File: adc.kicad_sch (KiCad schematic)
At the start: 9 parts, among them U801 AD7357xRU

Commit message: Combined update (kicad 6.0.4..) - Update schematic to kicad 6.0.4 - Assign footprints for SMA connectors - Replace MCP1825T with MCP1824T (chip shortages..)
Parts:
- renumbered C801 to C701, C802 to C702, C803 to C703, C804 to C704, C805 to C705, C806 to C706, C807 to C707, C808 to C708, U801 to U701
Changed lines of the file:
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@@
     (effects (font (size 1.27 1.27)) (justify right))
   )
-  (symbol (lib_id "symbols:+3.3VD") (at 167.64 38.1 0)
-    (in_bom yes) (on_board yes) (fields_autoplaced)
-    (property "Reference" "#PWR0810" (id 0) (at 167.64 41.91 0)
+  (symbol (lib_id "symbols:+3.3VD") (at 167.64 38.1 0) (unit 1)
+    (in_bom yes) (on_board yes) (fields_autoplaced)
+    (property "Reference" "#PWR0710" (id 0) (at 167.64 41.91 0)
       (effects (font (size 1.27 1.27)) hide)
     )
@@
     (pin "1")
   )
-  (symbol (lib_id "Device:C_Polarized") (at 120.65 125.73 0)
-    (in_bom yes) (on_board yes) (fields_autoplaced)
-    (property "Reference" "C802" (id 0) (at 123.571 124.0063 0)
+  (symbol (lib_id "Device:C_Polarized") (at 120.65 125.73 0) (unit 1)
+    (in_bom yes) (on_board yes) (fields_autoplaced)
+    (property "Reference" "C702" (id 0) (at 123.571 124.0063 0)
       (effects (font (size 1.27 1.27)) (justify left))
     )
@@
     (pin "2")
   )
-  (symbol (lib_id "Device:C") (at 133.35 95.25 0)
-    (in_bom yes) (on_board yes) (fields_autoplaced)
-    (property "Reference" "C803" (id 0) (at 136.271 94.4153 0)
+  (symbol (lib_id "Device:C") (at 133.35 95.25 0) (unit 1)
+    (in_bom yes) (on_board yes) (fields_autoplaced)
+    (property "Reference" "C703" (id 0) (at 136.271 94.4153 0)
       (effects (font (size 1.27 1.27)) (justify left))
     )
@@
     (pin "2")
   )
-  (symbol (lib_id "symbols:AD7357xRU") (at 158.75 101.6 0)
-    (in_bom yes) (on_board yes) (fields_autoplaced)
-    (property "Reference" "U801" (id 0) (at 164.5794 72.6272 0)
+  (symbol (lib_id "symbols:AD7357xRU") (at 158.75 101.6 0) (unit 1)
+    (in_bom yes) (on_board yes) (fields_autoplaced)
+    (property "Reference" "U701" (id 0) (at 164.5794 72.6272 0)
       (effects (font (size 1.27 1.27)) (justify left))
     )
@@
     (pin "9")
   )
-  (symbol (lib_id "power:GND") (at 120.65 130.81 0)
-    (in_bom yes) (on_board yes) (fields_autoplaced)
-    (property "Reference" "#PWR0802" (id 0) (at 120.65 137.16 0)
+  (symbol (lib_id "power:GND") (at 120.65 130.81 0) (unit 1)
+    (in_bom yes) (on_board yes) (fields_autoplaced)
+    (property "Reference" "#PWR0702" (id 0) (at 120.65 137.16 0)
       (effects (font (size 1.27 1.27)) hide)
     )
@@
     (pin "1")
   )
-  (symbol (lib_id "Device:C") (at 133.35 125.73 0)
-    (in_bom yes) (on_board yes) (fields_autoplaced)
-    (property "Reference" "C804" (id 0) (at 136.271 124.8953 0)
+  (symbol (lib_id "Device:C") (at 133.35 125.73 0) (unit 1)
+    (in_bom yes) (on_board yes) (fields_autoplaced)
+    (property "Reference" "C704" (id 0) (at 136.271 124.8953 0)
       (effects (font (size 1.27 1.27)) (justify left))
     )
@@
     (pin "2")
   )
-  (symbol (lib_id "power:GND") (at 120.65 100.33 0)
-    (in_bom yes) (on_board yes) (fields_autoplaced)
-    (property "Reference" "#PWR0801" (id 0) (at 120.65 106.68 0)
+  (symbol (lib_id "power:GND") (at 120.65 100.33 0) (unit 1)
+    (in_bom yes) (on_board yes) (fields_autoplaced)
+    (property "Reference" "#PWR0701" (id 0) (at 120.65 106.68 0)
       (effects (font (size 1.27 1.27)) hide)
     )
@@
     (pin "1")
   )
-  (symbol (lib_id "Device:C") (at 149.86 44.45 0)
-    (in_bom yes) (on_board yes) (fields_autoplaced)
-    (property "Reference" "C806" (id 0) (at 152.781 43.6153 0)
+  (symbol (lib_id "Device:C") (at 149.86 44.45 0) (unit 1)
+    (in_bom yes) (on_board yes) (fields_autoplaced)
+    (property "Reference" "C706" (id 0) (at 152.781 43.6153 0)
       (effects (font (size 1.27 1.27)) (justify left))
     )
@@
     (pin "2")
   )
-  (symbol (lib_id "power:GND") (at 149.86 50.8 0)
-    (in_bom yes) (on_board yes) (fields_autoplaced)
-    (property "Reference" "#PWR0806" (id 0) (at 149.86 57.15 0)
+  (symbol (lib_id "power:GND") (at 149.86 50.8 0) (unit 1)
+    (in_bom yes) (on_board yes) (fields_autoplaced)
+    (property "Reference" "#PWR0706" (id 0) (at 149.86 57.15 0)
       (effects (font (size 1.27 1.27)) hide)
     )
@@
     (pin "1")
   )
-  (symbol (lib_id "symbols:+2.5VA") (at 154.94 72.39 0)
-    (in_bom yes) (on_board yes) (fields_autoplaced)
-    (property "Reference" "#PWR0808" (id 0) (at 154.94 76.2 0)
+  (symbol (lib_id "symbols:+2.5VA") (at 154.94 72.39 0) (unit 1)
+    (in_bom yes) (on_board yes) (fields_autoplaced)
+    (property "Reference" "#PWR0708" (id 0) (at 154.94 76.2 0)
       (effects (font (size 1.27 1.27)) hide)
     )
@@
     (pin "1")
   )
-  (symbol (lib_id "symbols:+3.3VD") (at 162.56 72.39 0)
-    (in_bom yes) (on_board yes) (fields_autoplaced)
-    (property "Reference" "#PWR0809" (id 0) (at 162.56 76.2 0)
+  (symbol (lib_id "symbols:+3.3VD") (at 162.56 72.39 0) (unit 1)
+    (in_bom yes) (on_board yes) (fields_autoplaced)
+    (property "Reference" "#PWR0709" (id 0) (at 162.56 76.2 0)
       (effects (font (size 1.27 1.27)) hide)
     )
@@
     (pin "1")
   )
-  (symbol (lib_id "power:GND") (at 133.35 130.81 0)
-    (in_bom yes) (on_board yes) (fields_autoplaced)
-    (property "Reference" "#PWR0804" (id 0) (at 133.35 137.16 0)
+  (symbol (lib_id "power:GND") (at 133.35 130.81 0) (unit 1)
+    (in_bom yes) (on_board yes) (fields_autoplaced)
+    (property "Reference" "#PWR0704" (id 0) (at 133.35 137.16 0)
       (effects (font (size 1.27 1.27)) hide)
     )
@@
     (pin "1")
   )
-  (symbol (lib_id "power:GND") (at 167.64 50.8 0)
-    (in_bom yes) (on_board yes) (fields_autoplaced)
-    (property "Reference" "#PWR0811" (id 0) (at 167.64 57.15 0)
+  (symbol (lib_id "power:GND") (at 167.64 50.8 0) (unit 1)
+    (in_bom yes) (on_board yes) (fields_autoplaced)
+    (property "Reference" "#PWR0711" (id 0) (at 167.64 57.15 0)
       (effects (font (size 1.27 1.27)) hide)
     )
@@
     (pin "1")
   )
-  (symbol (lib_id "Device:C_Polarized") (at 120.65 95.25 0)
-    (in_bom yes) (on_board yes) (fields_autoplaced)
-    (property "Reference" "C801" (id 0) (at 123.571 93.5263 0)
+  (symbol (lib_id "Device:C_Polarized") (at 120.65 95.25 0) (unit 1)
+    (in_bom yes) (on_board yes) (fields_autoplaced)
+    (property "Reference" "C701" (id 0) (at 123.571 93.5263 0)
       (effects (font (size 1.27 1.27)) (justify left))
     )
@@
     (pin "2")
   )
-  (symbol (lib_id "symbols:+2.5VA") (at 149.86 38.1 0)
-    (in_bom yes) (on_board yes) (fields_autoplaced)
-    (property "Reference" "#PWR0805" (id 0) (at 149.86 41.91 0)
+  (symbol (lib_id "symbols:+2.5VA") (at 149.86 38.1 0) (unit 1)
+    (in_bom yes) (on_board yes) (fields_autoplaced)
+    (property "Reference" "#PWR0705" (id 0) (at 149.86 41.91 0)
       (effects (font (size 1.27 1.27)) hide)
     )
@@
     (pin "1")
   )
-  (symbol (lib_id "Device:C") (at 180.34 44.45 0)
-    (in_bom yes) (on_board yes) (fields_autoplaced)
-    (property "Reference" "C808" (id 0) (at 183.261 43.6153 0)
+  (symbol (lib_id "Device:C") (at 180.34 44.45 0) (unit 1)
+    (in_bom yes) (on_board yes) (fields_autoplaced)
+    (property "Reference" "C708" (id 0) (at 183.261 43.6153 0)
       (effects (font (size 1.27 1.27)) (justify left))
     )
@@
     (pin "2")
   )
-  (symbol (lib_id "Device:C") (at 167.64 44.45 0)
-    (in_bom yes) (on_board yes) (fields_autoplaced)
-    (property "Reference" "C807" (id 0) (at 170.561 43.6153 0)
+  (symbol (lib_id "Device:C") (at 167.64 44.45 0) (unit 1)
+    (in_bom yes) (on_board yes) (fields_autoplaced)
+    (property "Reference" "C707" (id 0) (at 170.561 43.6153 0)
       (effects (font (size 1.27 1.27)) (justify left))
     )
@@
     (pin "2")
   )
-  (symbol (lib_id "Device:C") (at 137.16 44.45 0)
-    (in_bom yes) (on_board yes) (fields_autoplaced)
-    (property "Reference" "C805" (id 0) (at 140.081 43.6153 0)
+  (symbol (lib_id "Device:C") (at 137.16 44.45 0) (unit 1)
+    (in_bom yes) (on_board yes) (fields_autoplaced)
+    (property "Reference" "C705" (id 0) (at 140.081 43.6153 0)
       (effects (font (size 1.27 1.27)) (justify left))
     )
@@
     (pin "2")
   )
-  (symbol (lib_id "power:GND") (at 153.67 132.08 0)
-    (in_bom yes) (on_board yes) (fields_autoplaced)
-    (property "Reference" "#PWR0807" (id 0) (at 153.67 138.43 0)
+  (symbol (lib_id "power:GND") (at 153.67 132.08 0) (unit 1)
+    (in_bom yes) (on_board yes) (fields_autoplaced)
+    (property "Reference" "#PWR0707" (id 0) (at 153.67 138.43 0)
       (effects (font (size 1.27 1.27)) hide)
     )
@@
     (pin "1")
   )
-  (symbol (lib_id "power:GND") (at 133.35 100.33 0)
-    (in_bom yes) (on_board yes) (fields_autoplaced)
-    (property "Reference" "#PWR0803" (id 0) (at 133.35 106.68 0)
-      (effects (font (size 1.27 1.27)) hide)
-    )
+  (symbol (lib_id "power:GND") (at 133.35 100.33 0) (unit 1)
+    (in_bom yes) (on_board yes) (fields_autoplaced)
+    (property "Reference" "#PWR0703" (id 0) (at 133.35 106.68 0)
+      (effects (font (size 1.27 1.27)) hide)
+    )

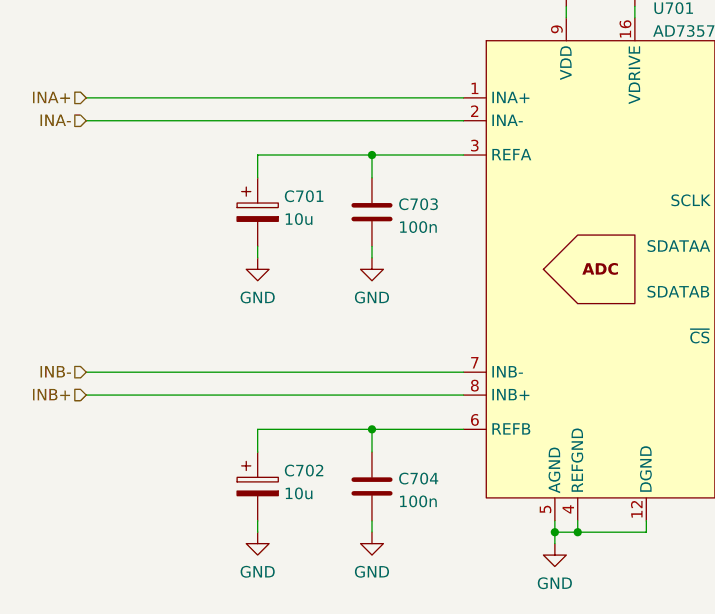
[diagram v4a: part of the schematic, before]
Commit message: Replace 10uf al-elco by tantalum -Space savings (0805 vs 4mm cylinder)
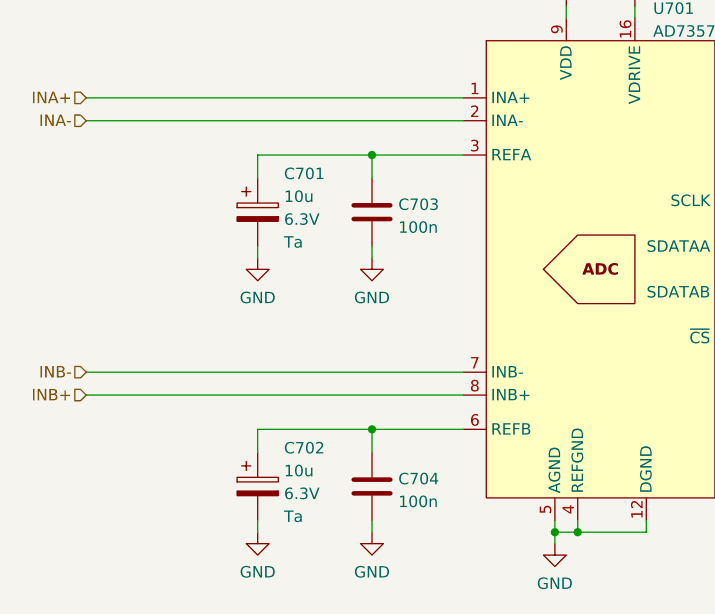
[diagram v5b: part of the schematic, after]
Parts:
- C701, C702: footprint Capacitor_SMD:CP_Elec_4x5.8 -> Capacitor_Tantalum_SMD:CP_EIA-2012-15_AVX-P; Mfr Nichicon -> AVX; Mfr PN UCL1C100MCL1GS -> TCJN106M006R0500; Spec1 (none) -> 6.3V; Spec2 (none) -> Ta
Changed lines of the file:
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@@
   (symbol (lib_id "Device:C_Polarized") (at 120.65 125.73 0) (unit 1)
     (in_bom yes) (on_board yes) (fields_autoplaced)
-    (property "Reference" "C702" (id 0) (at 123.571 124.0063 0)
-      (effects (font (size 1.27 1.27)) (justify left))
-    )
-    (property "Value" "10u" (id 1) (at 123.571 126.5432 0)
-      (effects (font (size 1.27 1.27)) (justify left))
-    )
-    (property "Footprint" "Capacitor_SMD:CP_Elec_4x5.8" (id 2) (at 121.6152 129.54 0)
+    (property "Reference" "C702" (id 0) (at 123.571 121.4694 0)
+      (effects (font (size 1.27 1.27)) (justify left))
+    )
+    (property "Value" "10u" (id 1) (at 123.571 124.0063 0)
+      (effects (font (size 1.27 1.27)) (justify left))
+    )
+    (property "Footprint" "Capacitor_Tantalum_SMD:CP_EIA-2012-15_AVX-P" (id 2) (at 121.6152 129.54 0)
       (effects (font (size 1.27 1.27)) hide)
     )
@@
       (effects (font (size 1.27 1.27)) hide)
     )
-    (property "Spec1" "" (id 4) (at 123.571 126.5432 0)
-      (effects (font (size 1.27 1.27)) (justify left))
-    )
-    (property "Spec2" "" (id 5) (at 123.571 129.0801 0)
-      (effects (font (size 1.27 1.27)) (justify left))
-    )
-    (property "Tolerance" "" (id 6) (at 120.65 125.73 0)
-      (effects (font (size 1.27 1.27)) hide)
-    )
-    (property "Mfr" "Nichicon" (id 7) (at 120.65 125.73 0)
-      (effects (font (size 1.27 1.27)) hide)
-    )
-    (property "Mfr PN" "UCL1C100MCL1GS" (id 8) (at 120.65 125.73 0)
+    (property "Spec1" "6.3V" (id 4) (at 123.571 126.5432 0)
+      (effects (font (size 1.27 1.27)) (justify left))
+    )
+    (property "Spec2" "Ta" (id 5) (at 123.571 129.0801 0)
+      (effects (font (size 1.27 1.27)) (justify left))
+    )
+    (property "Mfr" "AVX" (id 7) (at 120.65 125.73 0)
+      (effects (font (size 1.27 1.27)) hide)
+    )
+    (property "Mfr PN" "TCJN106M006R0500" (id 8) (at 120.65 125.73 0)
       (effects (font (size 1.27 1.27)) hide)
     )
@@
   (symbol (lib_id "Device:C_Polarized") (at 120.65 95.25 0) (unit 1)
     (in_bom yes) (on_board yes) (fields_autoplaced)
-    (property "Reference" "C701" (id 0) (at 123.571 93.5263 0)
-      (effects (font (size 1.27 1.27)) (justify left))
-    )
-    (property "Value" "10u" (id 1) (at 123.571 96.0632 0)
-      (effects (font (size 1.27 1.27)) (justify left))
-    )
-    (property "Footprint" "Capacitor_SMD:CP_Elec_4x5.8" (id 2) (at 121.6152 99.06 0)
+    (property "Reference" "C701" (id 0) (at 123.571 90.9894 0)
+      (effects (font (size 1.27 1.27)) (justify left))
+    )
+    (property "Value" "10u" (id 1) (at 123.571 93.5263 0)
+      (effects (font (size 1.27 1.27)) (justify left))
+    )
+    (property "Footprint" "Capacitor_Tantalum_SMD:CP_EIA-2012-15_AVX-P" (id 2) (at 121.6152 99.06 0)
       (effects (font (size 1.27 1.27)) hide)
     )
@@
       (effects (font (size 1.27 1.27)) hide)
     )
-    (property "Spec1" "" (id 4) (at 123.571 96.0632 0)
-      (effects (font (size 1.27 1.27)) (justify left))
-    )
-    (property "Spec2" "" (id 5) (at 123.571 98.6001 0)
-      (effects (font (size 1.27 1.27)) (justify left))
-    )
-    (property "Tolerance" "" (id 6) (at 120.65 95.25 0)
-      (effects (font (size 1.27 1.27)) hide)
-    )
-    (property "Mfr" "Nichicon" (id 7) (at 120.65 95.25 0)
-      (effects (font (size 1.27 1.27)) hide)
-    )
-    (property "Mfr PN" "UCL1C100MCL1GS" (id 8) (at 120.65 95.25 0)
-      (effects (font (size 1.27 1.27)) hide)
-    )
+    (property "Spec1" "6.3V" (id 4) (at 123.571 96.0632 0)
+      (effects (font (size 1.27 1.27)) (justify left))
+    )
+    (property "Spec2" "Ta" (id 5) (at 123.571 98.6001 0)
+      (effects (font (size 1.27 1.27)) (justify left))
+    )
+    (property "Mfr" "AVX" (id 7) (at 120.65 95.25 0)
+      (effects (font (size 1.27 1.27)) hide)
+    )
+    (property "Mfr PN" "TCJN106M006R0500" (id 8) (at 120.65 95.25 0)
+      (effects (font (size 1.27 1.27)) hide)
+    )
